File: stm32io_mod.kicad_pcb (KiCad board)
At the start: 2 copper layers, 70.5 x 73.7 mm, 48 parts, among them J1 UART, M1 BluePill, Q1 BC858, Q2 BC858, Q3 BC858, Q4 BC858, SW1 button_1, SW2 button_2, SW3 button_3, SW4 button_4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

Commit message: retoques finales
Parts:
- added REF**: MountingHole_2.7mm, MountingHole:MountingHole_2.7mm, F.Cu at (146.1, 92.2)
- added REF**: MountingHole_2.7mm, MountingHole:MountingHole_2.7mm, F.Cu at (113.3, 62.0)
- added REF**: MountingHole_2.7mm, MountingHole:MountingHole_2.7mm, F.Cu at (113.3, 128.5)
- added REF**: MountingHole_2.7mm, MountingHole:MountingHole_2.7mm, F.Cu at (176.8, 128.5)
- added REF**: MountingHole_2.7mm, MountingHole:MountingHole_2.7mm, F.Cu at (176.8, 62.0)
- moved R25 3.67 mm to (146.3, 88.1), turned to 0 degrees
- moved R14 2.54 mm to (147.3, 84.8)
- moved R13 2.54 mm to (144.7, 84.8)
- moved R16 2.54 mm to (149.7, 84.8)
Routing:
- net GND: track 53.2 -> 42.4 mm, vias 2 -> 0
- net led4: track 18.8 -> 13.3 mm
- net VCC: track 188.5 -> 192.9 mm
- net rotB: track 27.1 -> 25.8 mm
- net rotA: track 20.8 -> 19.5 mm
- net swr: track 45.7 -> 44.8 mm
- net Net-(D5-Pad1): track 38.9 -> 38.2 mm

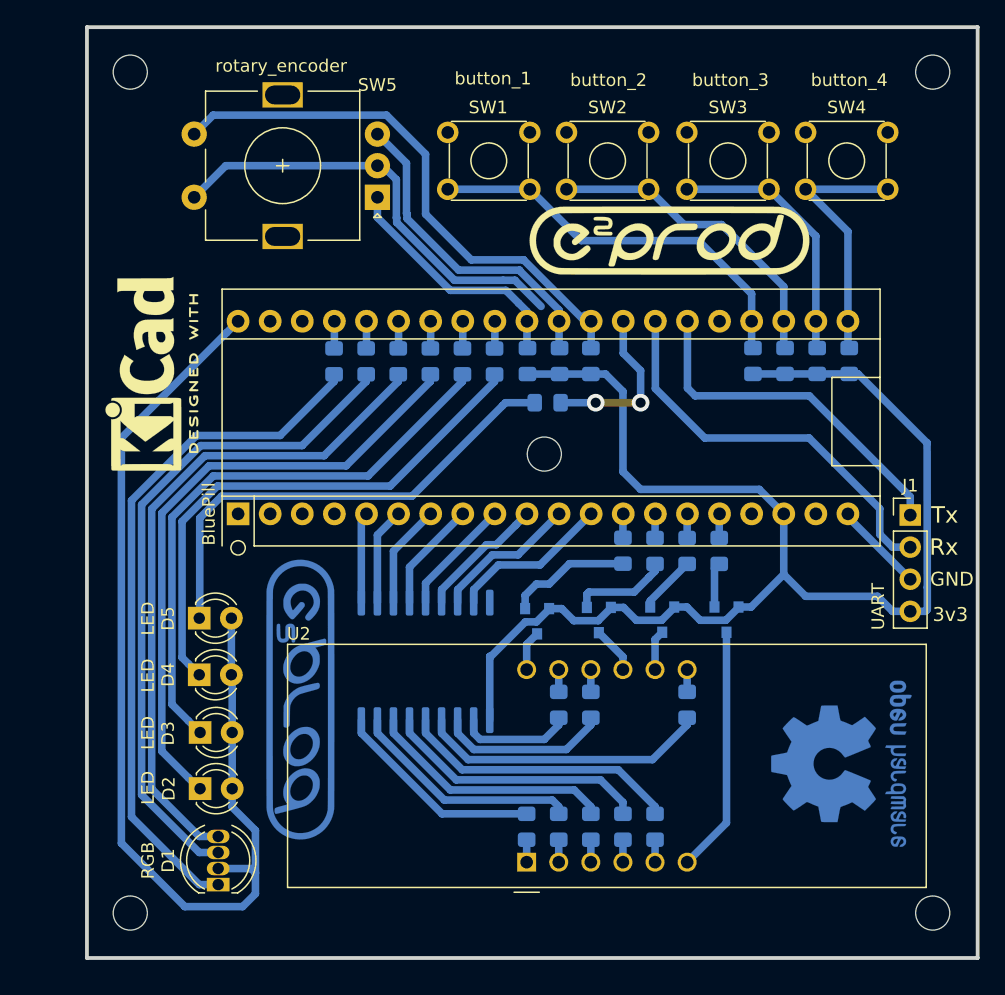
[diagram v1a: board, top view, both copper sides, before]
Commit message: Se mejoró el plano de masa
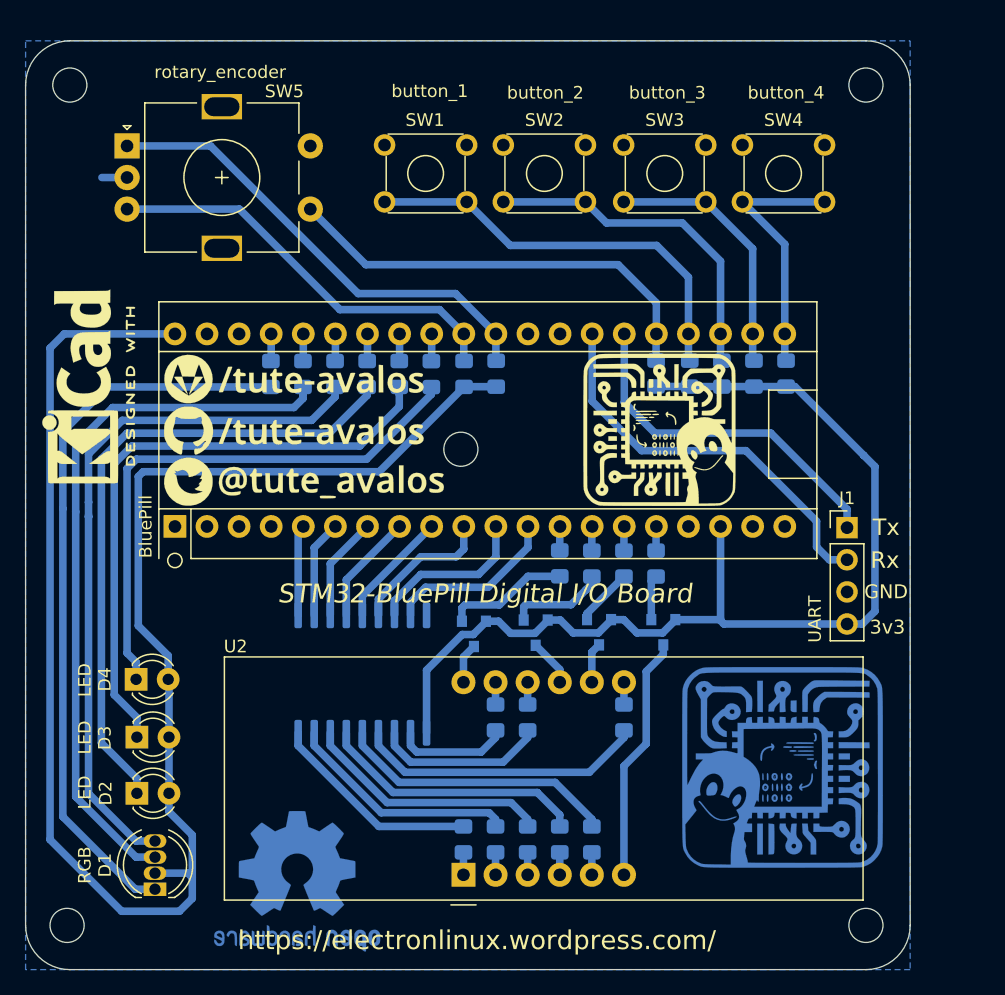
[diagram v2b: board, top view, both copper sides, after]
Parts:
- removed D5: LED, LED_THT:LED_D3.0mm_Clear
- removed G***: LOGO, e2prod:e2prod-silks
- removed G***: LOGO, e2prod:e2prod-cu
- removed R25: 100Ω, Resistor_SMD:R_0805_2012Metric_Pad1.15x1.40mm_HandSolder
- removed the REF** at (146.1, 92.2)
- removed the REF** at (113.3, 62.0)
- removed the REF** at (113.3, 128.5)
- removed the REF** at (176.8, 128.5)
- removed the REF** at (176.8, 62.0)
- added ElectronLinux: LOGO, electronlinux:electronlinux-cu, B.Cu at (164.9, 117.0)
- added ElectronLinux: LOGO, electronlinux:electronlinux-silks_12mm, F.Cu at (155.2, 90.3)
- added REF**: MountingHole_2.7mm, MountingHole:MountingHole_2.7mm, F.Cu at (171.5, 129.5)
- added REF**: MountingHole_2.7mm, MountingHole:MountingHole_2.7mm, F.Cu at (171.5, 63.0)
- added REF**: MountingHole_2.7mm, MountingHole:MountingHole_2.7mm, F.Cu at (139.4, 91.8)
- added REF**: MountingHole_2.7mm, MountingHole:MountingHole_2.7mm, F.Cu at (108.5, 63.0)
- added REF**: MountingHole_2.7mm, MountingHole:MountingHole_2.7mm, F.Cu at (108.3, 129.5)
- added Social: Links, electronlinux:electronlinux-social-22x12, F.Cu at (127.0, 90.3)
- moved REF** 44.0 mm to (126.5, 126.0), turned to 180 degrees
- moved SW5 20.2 mm to (113.0, 67.8), turned to 0 degrees
- moved R14 7.62 mm to (139.7, 85.9)
- moved R16 5.25 mm to (154.9, 85.8)
- moved J1 5.10 mm to (170.0, 98.0)
- moved M1 5.10 mm to (116.8, 97.9)
- moved Q1 5.10 mm to (140.5, 106.4)
- moved Q2 5.10 mm to (145.4, 106.3)
- moved Q3 5.10 mm to (150.4, 106.3)
- moved Q4 5.10 mm to (155.5, 106.3)
- moved R1 5.10 mm to (157.6, 85.8)
- moved R10 5.10 mm to (144.7, 122.7)
- moved R11 5.10 mm to (160.1, 85.8)
- moved R12 5.10 mm to (165.2, 85.8)
- moved R17 5.10 mm to (124.4, 85.9)
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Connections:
- M1 pad 1: (no net) -> Net-(M1-Pad1)
- M1 pad 17: (no net) -> Net-(M1-Pad17)
- M1 pad 2: (no net) -> Net-(M1-Pad2)
- M1 pad 25: (no net) -> swr
- M1 pad 28: led4 -> Net-(M1-Pad28)
- M1 pad 29: swr -> Net-(M1-Pad29)
- M1 pad 3: (no net) -> Net-(M1-Pad3)
- M1 pad 30: rotB -> rotA
- M1 pad 31: rotA -> rotB
- M1 pad 38: (no net) -> Net-(M1-Pad38)
- M1 pad 4: (no net) -> Net-(M1-Pad4)
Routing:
- net GND: track 42.4 -> 1.99 mm
- net Net-(D5-Pad1): track 38.2 -> 0.00 mm
- net VCC: track 192.9 -> 216.9 mm
- net rotA: track 19.5 -> 37.5 mm
- net led4: track 13.3 -> 0.00 mm, vias 2 -> 0
- net swr: track 44.8 -> 35.0 mm
- net rotB: track 25.8 -> 32.9 mm
- net Net-(D1-Pad3): track 53.3 -> 57.1 mm
- net Net-(D1-Pad1): track 54.6 -> 58.1 mm
- net Net-(D3-Pad1): track 45.9 -> 48.9 mm
- net Net-(D2-Pad1): track 49.2 -> 52.0 mm
- net Net-(D1-Pad4): track 53.2 -> 56.0 mm
- net Net-(M1-Pad11): track 11.5 -> 14.1 mm
- net Net-(M1-Pad10): track 10.3 -> 12.5 mm
- net sw2: track 25.3 -> 27.1 mm
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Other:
- board size 70.5 x 73.7 mm -> 70 x 73.5 mm
- board text added: "STM32-BluePill Digital I/O Board"
- board text added: "https://electronlinux.wordpress.com/"

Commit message: se actualizan las serigrafías a nuevos logos y nueva url
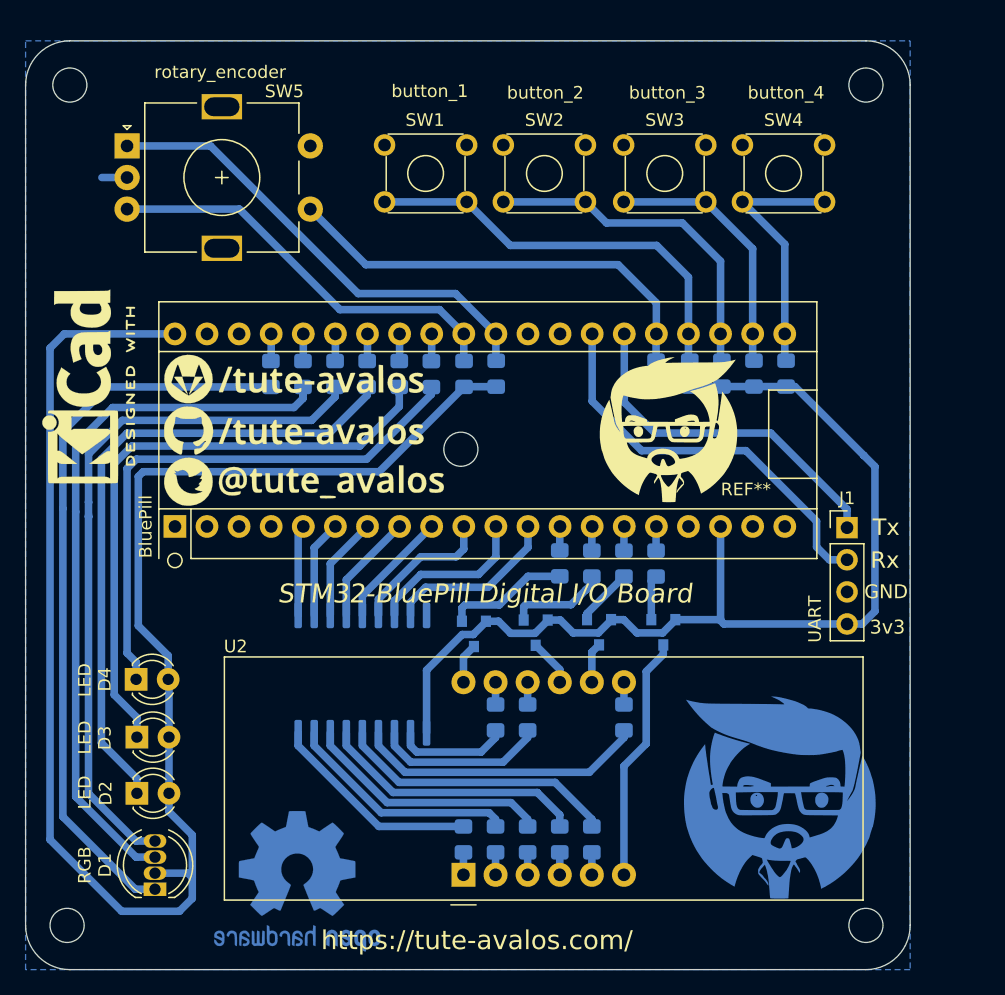
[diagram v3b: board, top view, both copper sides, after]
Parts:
- removed ElectronLinux: LOGO, electronlinux:electronlinux-cu
- removed ElectronLinux: LOGO, electronlinux:electronlinux-silks_12mm
- added REF**: tute-avalos-sliks, electronlinux:tute-avalos-sliks, F.Cu at (156.0, 91.0)
- added REF**: tute-avalos-cu_16mm, electronlinux:tute-avalos-cu_16mm, B.Cu at (165.0, 120.0)
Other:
- net class Default removed
- board text added: "MIT License Copyright (c) 2020-2025 Matías S. Ávalos (msavalos@gmail.com) Permission is hereby granted, free of charge, to any person obtaining a copy of this software and associated documentation files (the {dblquote}Software{dblquote}), to deal in the Software without restriction, including without limitation the rights to use, copy, modify, merge, publish, distribute, sublicense, and/or sell c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"
- board text added: "https://tute-avalos.com/"
- board text removed: "MIT License Copyright (c) 2020 Matías S. Ávalos (msavalos@gmail.com) Permission is hereby granted, free of charge, to any person obtaining a copy of this software and associated documentation files (the "Software"), to deal in the Software without restriction, including without limitation the rights to use, copy, modify, merge, publish, distribute, sublicense, and/or sell copies of the Software, 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"
- board text removed: "https://electronlinux.wordpress.com/"
